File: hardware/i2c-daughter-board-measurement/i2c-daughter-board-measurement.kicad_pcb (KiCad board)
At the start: 2 copper layers, 75 x 60 mm, 12 parts, among them J1 Conn_01x04, U5 PCF8574

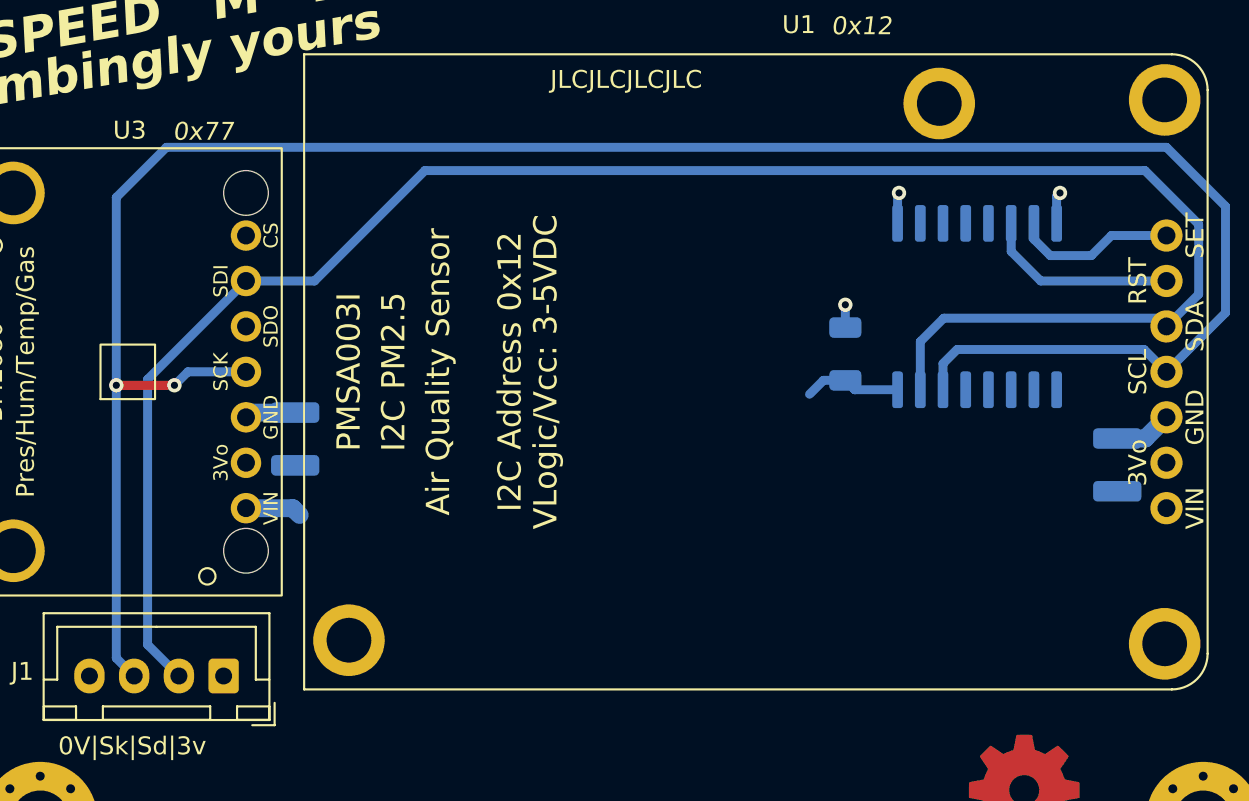
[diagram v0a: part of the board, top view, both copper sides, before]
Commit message: Updating images & 3d models
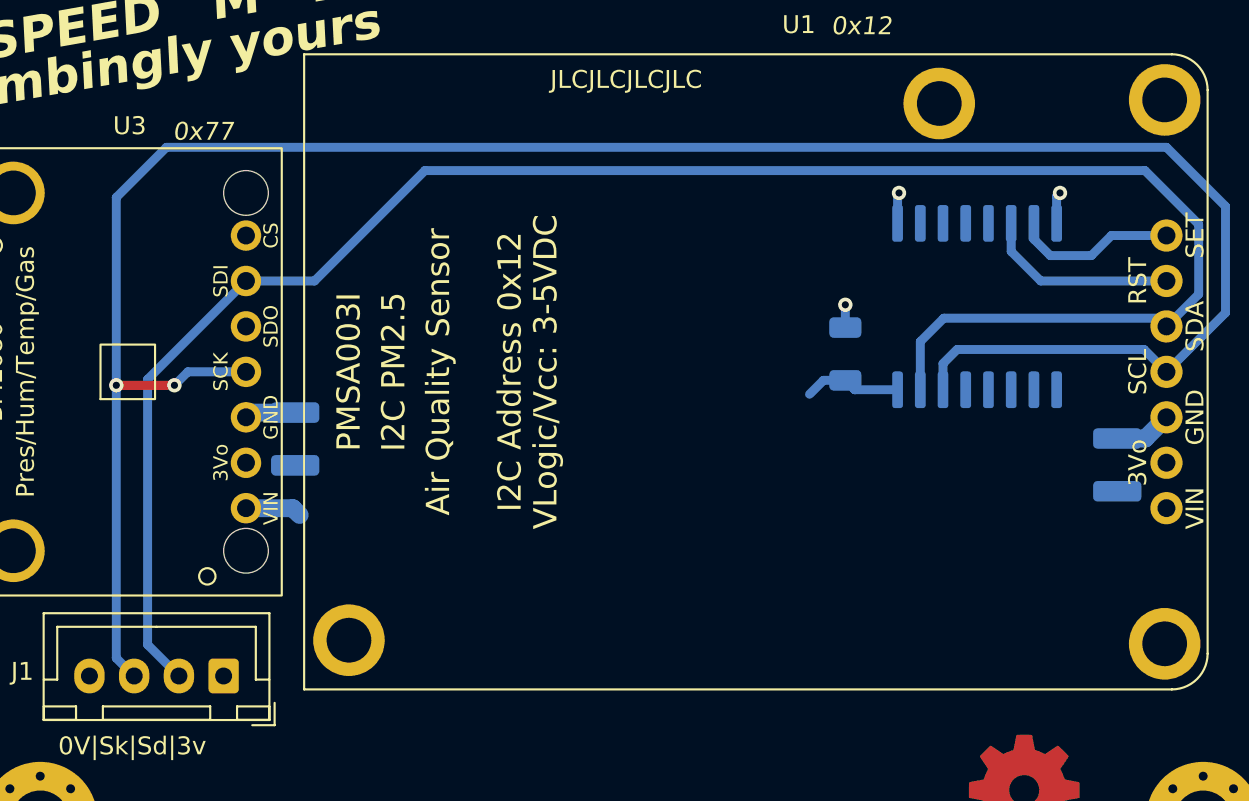
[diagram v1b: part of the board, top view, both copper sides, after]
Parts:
- U3: footprint breakboard:bme680 -> additional:bme680
